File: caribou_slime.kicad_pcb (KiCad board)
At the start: 2 copper layers, 62.8 x 37.6 mm, 14 parts, among them J1 Conn_01x02_MountingPin, U1 ESP32-C3_SUPERMINI, U2 BMI270, U3 TP4056

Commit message: chore(pcb): Remove TP4056 board
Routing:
- net unconnected-(U3---Pad2): track 43.4 -> 0.00 mm, vias 1 -> 0
- net /B+: track 0.00 -> 43.4 mm, vias 0 -> 1
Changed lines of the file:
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@@
   (net 25 "Net-(U3-OUT-)")
   (net 26 "unconnected-(S1-Pad3)")
-  (net 27 "unconnected-(U3---Pad2)")
-  (net 28 "/B+")
-  (net 29 "/B-")
+  (net 27 "/B+")
+  (net 28 "/B-")
   (footprint "Connector_JST:JST_PH_B2B-PH-K_1x02_P2.00mm_Vertical" (layer "F.Cu")
     (at 38.846 52.112 180)
@@
       (stroke (width 0.1) (type solid)) (layer "F.Fab"))
     (pad "1" thru_hole roundrect (at 0 0 180) (size 1.2 1.75) (drill 0.75) (layers "*.Cu" "*.Mask") (roundrect_rratio 0.208333)
-      (net 29 "/B-") (pinfunction "Pin_1") (pintype "passive"))
+      (net 28 "/B-") (pinfunction "Pin_1") (pintype "passive"))
     (pad "2" thru_hole oval (at 2 0 180) (size 1.2 1.75) (drill 0.75) (layers "*.Cu" "*.Mask")
-      (net 28 "/B+") (pinfunction "Pin_2") (pintype "passive"))
+      (net 27 "/B+") (pinfunction "Pin_2") (pintype "passive"))
     (model "${KICAD6_3DMODEL_DIR}/Connector_JST.3dshapes/JST_PH_B2B-PH-K_1x02_P2.00mm_Vertical.wrl"
       (offset (xyz 0 0 0))

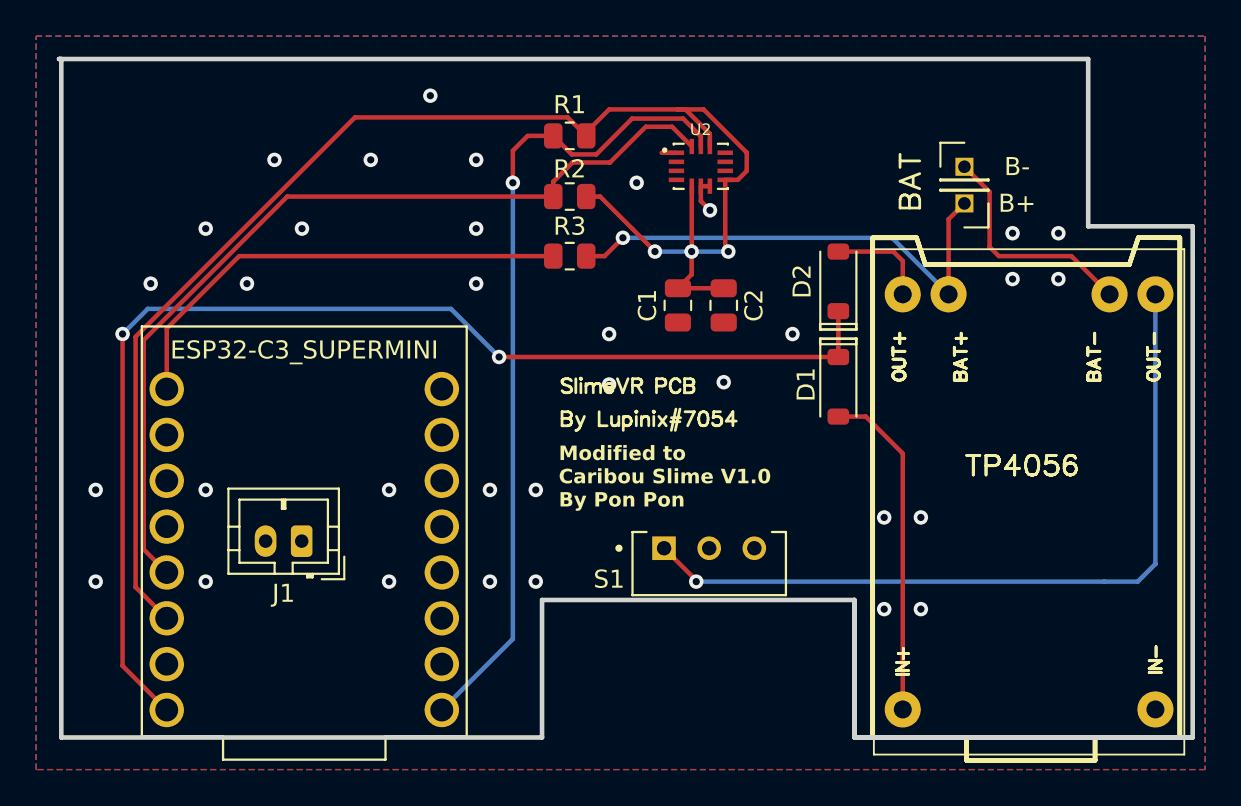
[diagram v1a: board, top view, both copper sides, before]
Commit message: chore(pcb): Cleanup after V1 and rebase
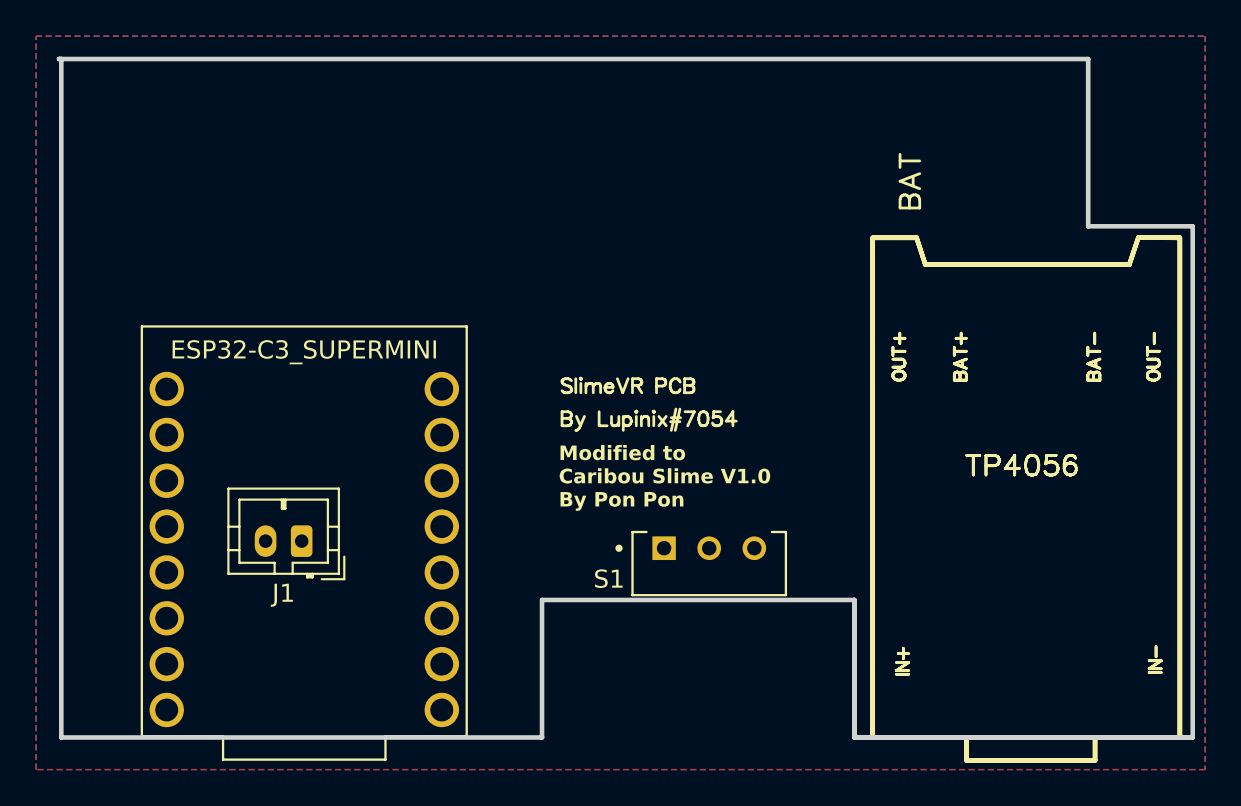
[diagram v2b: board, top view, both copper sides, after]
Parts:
- removed C1, C2: 100nF, Capacitor_SMD:C_0805_2012Metric
- removed D1, D2: B5817W, Diode_SMD:D_SOD-123
- removed H1: B+, Connector_PinHeader_2.54mm:PinHeader_1x01_P2.54mm_Vertical
- removed H2: B-, Connector_PinHeader_2.54mm:PinHeader_1x01_P2.54mm_Vertical
- removed R1, R2: 10k, Resistor_SMD:R_0805_2012Metric
- removed R3: 180k, Resistor_SMD:R_0805_2012Metric
- removed U2: BMI270, BMI270:XDCR_BMI270
- removed U3: TP4056, TP4056_Charging_Board:TP4056 Charging Board
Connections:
- S1 pad 1: Net-(U3-OUT-) -> (no net)
- S1 pad 3: unconnected-(S1-Pad3) -> (no net)
- U1 pad 0: Net-(U1-GPIO0) -> (no net)
- U1 pad 4: SDA -> (no net)
- U1 pad 5: SCL -> (no net)
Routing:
- net +3V3: track 84.6 -> 0.00 mm, vias 3 -> 0
- net +5V: track 65.7 -> 0.00 mm, vias 2 -> 0
- net Net-(U3-OUT-): track 49.6 -> 0.00 mm
- net SDA: track 45.6 -> 0.00 mm, vias 1 -> 0
- net /B+: track 43.4 -> 0.00 mm, vias 1 -> 0
- net unconnected-(U2-ASDX-Pad2): track 27.2 -> 0.00 mm, vias 1 -> 0
- net unconnected-(S1-Pad3): track 26.4 -> 0.00 mm
- net Net-(D1-A): track 18.6 -> 0.00 mm
- net unconnected-(U2-INT2-Pad9): track 12.8 -> 0.00 mm
- net Net-(D2-A): track 5.63 -> 0.00 mm
- net GND: track 3.23 -> 0.00 mm, vias 34 -> 0

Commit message: feat(pcb): Create initial V2 Hyperion layout
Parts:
- added C1: 100nF, Capacitor_SMD:C_0805_2012Metric, F.Cu at (72.4, 33.7)
- added C2: 100nF, Capacitor_SMD:C_0805_2012Metric, F.Cu at (56.9, 49.5)
- added C3: 100nF, Capacitor_SMD:C_0805_2012Metric, F.Cu at (54.9, 49.5)
- added C4: 10uF, Capacitor_SMD:C_0805_2012Metric, F.Cu at (84.9, 46.0)
- added C5: 10uF, Capacitor_SMD:C_0805_2012Metric, F.Cu at (57.2, 36.4)
- added C6: 10uF, Capacitor_SMD:C_0805_2012Metric, F.Cu at (60.5, 36.4)
- added D1: RED, Diode_SMD:D_0805_2012Metric, F.Cu at (72.5, 55.4)
- added D2: GRE, Diode_SMD:D_0805_2012Metric, F.Cu at (72.5, 50.8)
- added D3: B5817W, Diode_SMD:D_0805_2012Metric, F.Cu at (51.1, 28.3)
- added D4: B5817W, Diode_SMD:D_0805_2012Metric, F.Cu at (48.3, 32.3)
- added Q1: AO3145, Package_TO_SOT_SMD:SOT-23, F.Cu at (51.2, 32.3)
- added R1: 180k, Resistor_SMD:R_0805_2012Metric, F.Cu at (27.7, 42.8)
- added R10: 1k, Resistor_SMD:R_0805_2012Metric, F.Cu at (76.0, 57.4)
- added R11: 100, Resistor_SMD:R_0805_2012Metric, F.Cu at (79.6, 60.7)
- added R12: 100, Resistor_SMD:R_0805_2012Metric, F.Cu at (79.6, 50.8)
- added R13: 1k, Resistor_SMD:R_0805_2012Metric, F.Cu at (76.0, 50.8)
- added R14: 100, Resistor_SMD:R_0805_2012Metric, F.Cu at (79.6, 54.1)
- added R15: 180k, Resistor_SMD:R_0805_2012Metric, F.Cu at (54.1, 32.3)
- added R2: 10k, Resistor_SMD:R_0805_2012Metric, F.Cu at (52.2, 42.9)
- added R3: 10k, Resistor_SMD:R_0805_2012Metric, F.Cu at (52.2, 39.6)
- added R4: 100, Resistor_SMD:R_0805_2012Metric, F.Cu at (77.0, 35.3)
- added R5: 1k, Resistor_SMD:R_0805_2012Metric, F.Cu at (66.2, 34.5)
- added R6: 1k, Resistor_SMD:R_0805_2012Metric, F.Cu at (72.2, 43.4)
- added R7: 1k, Resistor_SMD:R_0805_2012Metric, F.Cu at (68.8, 43.4)
- added R8: 1k, Resistor_SMD:R_0805_2012Metric, F.Cu at (68.8, 46.7)
- added R9: 100, Resistor_SMD:R_0805_2012Metric, F.Cu at (79.6, 57.4)
- added U2: BMI270, BMI270:XDCR_BMI270, F.Cu at (55.5, 45.4)
- added U3: FS312F-G, Package_TO_SOT_SMD:TSOT-23-6, F.Cu at (71.4, 30.2)
- added U4: FS8205A, Package_SO:TSSOP-8_4.4x3mm_P0.65mm, F.Cu at (66.3, 29.7)
- added U5: TP4056, Package_SO:HSOP-8-1EP_3.9x4.9mm_P1.27mm_EP2.3x2.3mm, F.Cu at (79.1, 44.1)
- added U6: ME6211C33M5G, Package_TO_SOT_SMD:TSOT-23-5, F.Cu at (58.3, 32.5)
- J1: value Conn_01x02_MountingPin -> BATT JST
- moved J1 47.3 mm to (80.3, 29.2), turned to -90 degrees
- moved S1 1.65 mm to (60.8, 54.0)
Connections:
- J1 pad 1: /B- -> Net-(J1-Pin_1)
- J1 pad 2: /B+ -> VBAT
- S1 pad 1: (no net) -> VBAT
- S1 pad 2: GND -> Net-(D3-A)
- S1 pad 3: (no net) -> unconnected-(S1A-C-Pad3)
- U1 pad 0: (no net) -> Net-(U1-GPIO0)
- U1 pad 4: (no net) -> SDA
- U1 pad 5: (no net) -> SCL
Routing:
- net VBAT: track 0.00 -> 92.4 mm, vias 0 -> 1
- net +3V3: track 0.00 -> 78.8 mm, vias 0 -> 1
- net +5V: track 0.00 -> 76.4 mm, vias 0 -> 3
- net SDA: track 0.00 -> 54.3 mm, vias 0 -> 2
- net Net-(D3-A): track 0.00 -> 42.4 mm, vias 0 -> 2
- net SCL: track 0.00 -> 35.7 mm, vias 0 -> 1
- net Net-(U5-CHRG): track 0.00 -> 27.6 mm, vias 0 -> 2
- net Net-(U5-STDBY): track 0.00 -> 18.1 mm, vias 0 -> 2
- net GND: track 0.00 -> 15.1 mm, vias 0 -> 41
- net Net-(D4-K): track 0.00 -> 14.9 mm, vias 0 -> 2
- net Net-(U3-OD): track 0.00 -> 9.58 mm, vias 0 -> 2
- net Net-(U3-Vcc): track 0.00 -> 9.37 mm
- net Net-(U3-OC): track 0.00 -> 8.57 mm, vias 0 -> 2
- net Net-(U3-CS): track 0.00 -> 6.59 mm
- net Net-(R12-Pad2): track 0.00 -> 5.03 mm
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- added copper zone on B.Cu, net Net-(J1-Pin_1)
- added copper zone on F.Cu, net Net-(J1-Pin_1)
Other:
- board text added: "Modified to Caribou Slime V2.0 By Pon Pon"
- board text removed: "Modified to Caribou Slime V1.0 By Pon Pon"

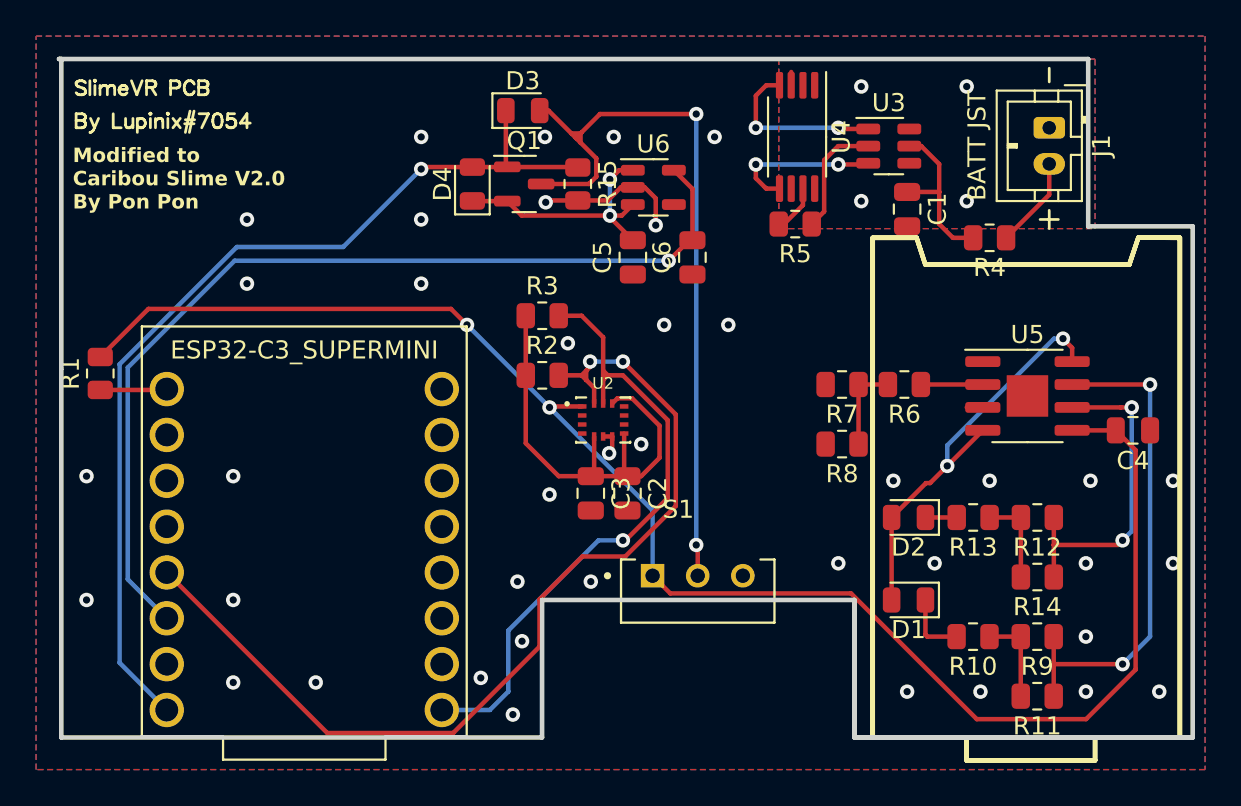
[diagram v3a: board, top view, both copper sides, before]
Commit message: fix(pcb): Remove doglegs from capacitor routing
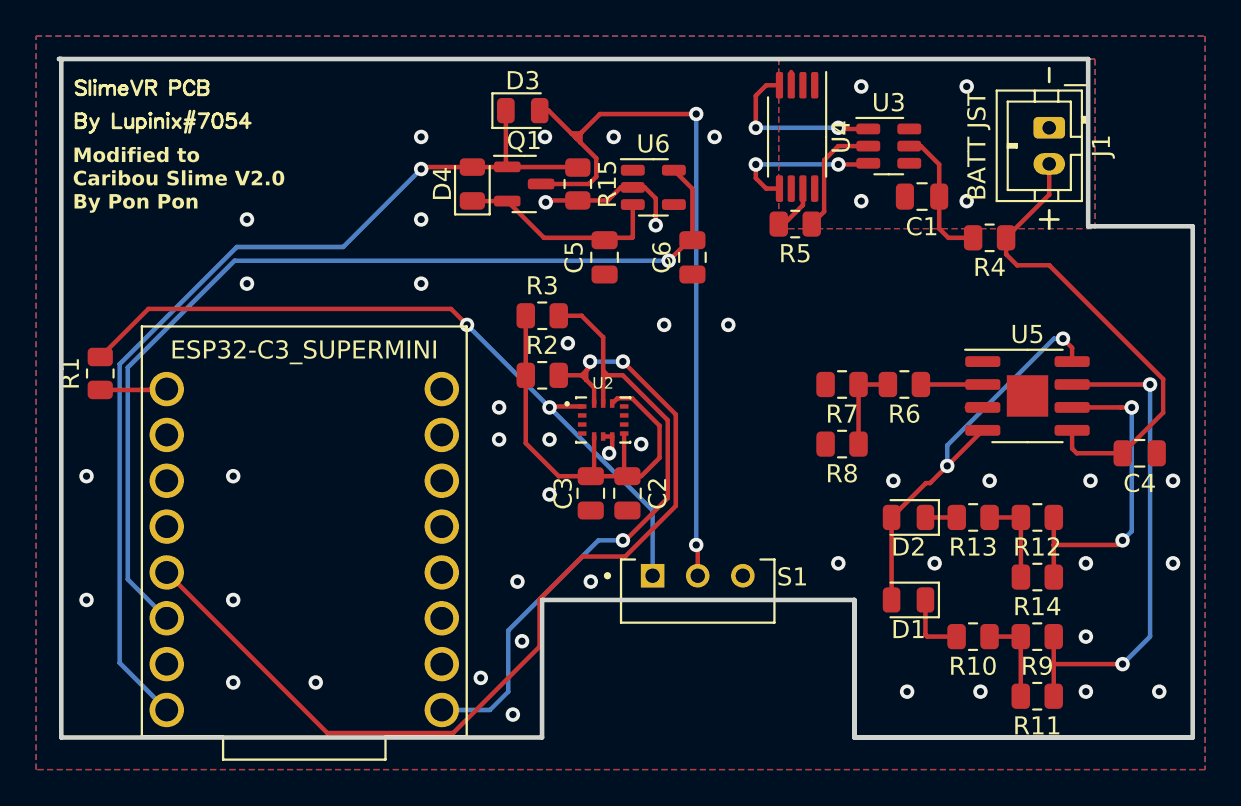
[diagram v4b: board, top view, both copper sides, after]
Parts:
- moved C5 1.57 mm to (55.6, 36.4)
- moved C4 1.32 mm to (85.3, 47.2)
- moved C1 1.08 mm to (73.2, 33.0), turned to 180 degrees
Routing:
- net VBAT: track 92.4 -> 66.5 mm
- net Net-(D4-K): track 14.9 -> 11.6 mm, vias 2 -> 0
- net Net-(U3-Vcc): track 9.37 -> 7.73 mm
- net GND: vias 41 -> 44
